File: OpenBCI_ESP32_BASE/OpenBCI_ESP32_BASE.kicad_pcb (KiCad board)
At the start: 2 copper layers, 50 x 50 mm, 43 parts, among them J1 Conn_01x02, J2 Conn_02x03_Odd_Even, J3 Conn_02x02_Odd_Even, J4 Conn_02x08_Odd_Even, SW1 SW_SPST, U1 LIS3DH, U10 TPS72325, U2 ESP32-DevKitC, U8 TPS60403, U9 TPS73225

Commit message: Latest PCB file and firmware
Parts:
- added R1: NF, Resistor_SMD:R_0603_1608Metric, F.Cu at (112.6, 57.8)
- added R2: NF, Resistor_SMD:R_0603_1608Metric, F.Cu at (125.0, 94.0)
- C1, C2, C3: value C -> 10u
- C35, C36, C37, C38, C39, C41, C42, C43: footprint Capacitor_SMD:C_0805_2012Metric -> Capacitor_SMD:C_0603_1608Metric
- C4: value C -> 0.1u; footprint Capacitor_SMD:C_0805_2012Metric -> Capacitor_SMD:C_0603_1608Metric
- J1: footprint Connector_JST:JST_PH_S2B-PH-K_1x02_P2.00mm_Horizontal -> Connector_JST:JST_PH_S2B-PH-SM4-TB_1x02-1MP_P2.00mm_Horizontal
- SW1: value SW_SPST -> SW_SPDT; footprint OpenBCI_ESP32:SW_SPDT_CK-JS102011SAQN -> Button_Switch_SMD:SW_SPDT_CK-JS102011SAQN
- moved J1 2.28 mm to (137.6, 55.1)
- moved C50 1.94 mm to (103.9, 60.8)
- moved C33 1.70 mm to (124.1, 61.1)
- moved C34 1.70 mm to (127.3, 62.3)
- moved L1 1.70 mm to (127.3, 60.3)
- moved D1 1.70 mm to (130.8, 59.6)
- moved SW1 1.70 mm to (126.0, 52.3)
- moved U2 0.40 mm to (148.5, 65.3)
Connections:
- J2 pad 5: Net-(J2-Pad5) -> unconnected-(J2-Pad5)
- J4 pad 12: Net-(J4-Pad12) -> unconnected-(J4-Pad12)
- J4 pad 13: Net-(J4-Pad13) -> unconnected-(J4-Pad13)
- J4 pad 5: Net-(J4-Pad5) -> unconnected-(J4-Pad5)
- J4 pad 7: Net-(J4-Pad7) -> unconnected-(J4-Pad7)
- SW1 pad 3: (no net) -> unconnected-(SW1-Pad3)
- U1 pad 11: Net-(U1-Pad11) -> /OpenBCI_ESP_DEVKIT/INT1
- U1 pad 2: Net-(U1-Pad2) -> unconnected-(U1-Pad2)
- U1 pad 3: Net-(U1-Pad3) -> unconnected-(U1-Pad3)
- U1 pad 7: Net-(U1-Pad7) -> unconnected-(U1-Pad7)
- U1 pad 9: Net-(U1-Pad9) -> unconnected-(U1-Pad9)
- U2 pad 11: Net-(U2-Pad11) -> /OpenBCI_ESP_DEVKIT/INT1
- U2 pad 16: Net-(U2-Pad16) -> unconnected-(U2-Pad16)
- U2 pad 17: Net-(U2-Pad17) -> unconnected-(U2-Pad17)
- U2 pad 18: Net-(U2-Pad18) -> unconnected-(U2-Pad18)
- U2 pad 2: Net-(U2-Pad2) -> unconnected-(U2-Pad2)
- U2 pad 20: Net-(U2-Pad20) -> unconnected-(U2-Pad20)
- U2 pad 21: Net-(U2-Pad21) -> unconnected-(U2-Pad21)
- U2 pad 22: Net-(U2-Pad22) -> unconnected-(U2-Pad22)
- U2 pad 24: Net-(U2-Pad24) -> unconnected-(U2-Pad24)
- U2 pad 25: Net-(U2-Pad25) -> unconnected-(U2-Pad25)
- U2 pad 26: Net-(U2-Pad26) -> unconnected-(U2-Pad26)
- U2 pad 34: Net-(U2-Pad34) -> unconnected-(U2-Pad34)
- U2 pad 35: Net-(U2-Pad35) -> unconnected-(U2-Pad35)
- U2 pad 38: Net-(U2-Pad38) -> GND
- U2 pad 4: Net-(U2-Pad4) -> unconnected-(U2-Pad4)
- U2 pad 5: Net-(U2-Pad5) -> unconnected-(U2-Pad5)
- U2 pad 6: Net-(U2-Pad6) -> unconnected-(U2-Pad6)
- U2 pad 7: Net-(U2-Pad7) -> /OpenBCI_ESP_DEVKIT/SDCD
- U2 pad 8: Net-(U2-Pad8) -> unconnected-(U2-Pad8)
- XS1 pad 1: Net-(XS1-Pad1) -> unconnected-(XS1-Pad1)
- XS1 pad 8: Net-(XS1-Pad8) -> unconnected-(XS1-Pad8)
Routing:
- net /OpenBCI_ESP_DEVKIT/INT1: track 0.00 -> 28.7 mm, vias 0 -> 3
- net /OpenBCI_ESP_DEVKIT/SDCD: track 0.00 -> 24.8 mm, vias 0 -> 1
- net GND: track 127.8 -> 118.4 mm
- net Net-(C42-Pad1): track 7.21 -> 12.4 mm
- net -2V5: track 49.4 -> 45.6 mm
- net Net-(J1-Pad1): track 9.86 -> 12.9 mm
- net Net-(C43-Pad1): track 7.76 -> 10.6 mm
- net Net-(C39-Pad1): track 2.21 -> 4.21 mm
- net +5V: track 39.3 -> 37.4 mm
- net +2V5: track 18.4 -> 16.7 mm
- net Net-(C40-Pad1): track 1.93 -> 3.53 mm
- net +3V3: track 77.6 -> 76.1 mm
- net Net-(C34-Pad1): track 40.8 -> 39.4 mm
- net /OpenBCI_ESP_DEVKIT/SCL: track 18.4 -> 17.6 mm
- net -5V: track 23.9 -> 23.3 mm
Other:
- net class Default removed

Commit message: Firmware updates
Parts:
- added R3: 4k7, Resistor_SMD:R_0603_1608Metric, F.Cu at (133.4, 80.7)
- added R4: 4k7, Resistor_SMD:R_0603_1608Metric, F.Cu at (135.2, 80.7)
- added R5: 220k, Resistor_SMD:R_0603_1608Metric, F.Cu at (137.1, 61.4)
- added R6: 120k, Resistor_SMD:R_0603_1608Metric, F.Cu at (141.1, 61.4)
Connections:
- U2 pad 3: /OpenBCI_ESP_DEVKIT/BATT -> Net-(U2-Pad3)
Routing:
- net Net-(U2-Pad3): track 0.00 -> 7.61 mm
- net +5V: track 37.4 -> 42.9 mm
- net /OpenBCI_ESP_DEVKIT/SDA: track 11.6 -> 15.9 mm
- net +3V3: track 76.1 -> 73.2 mm, vias 4 -> 5
- net /OpenBCI_ESP_DEVKIT/SCL: track 17.6 -> 20.0 mm

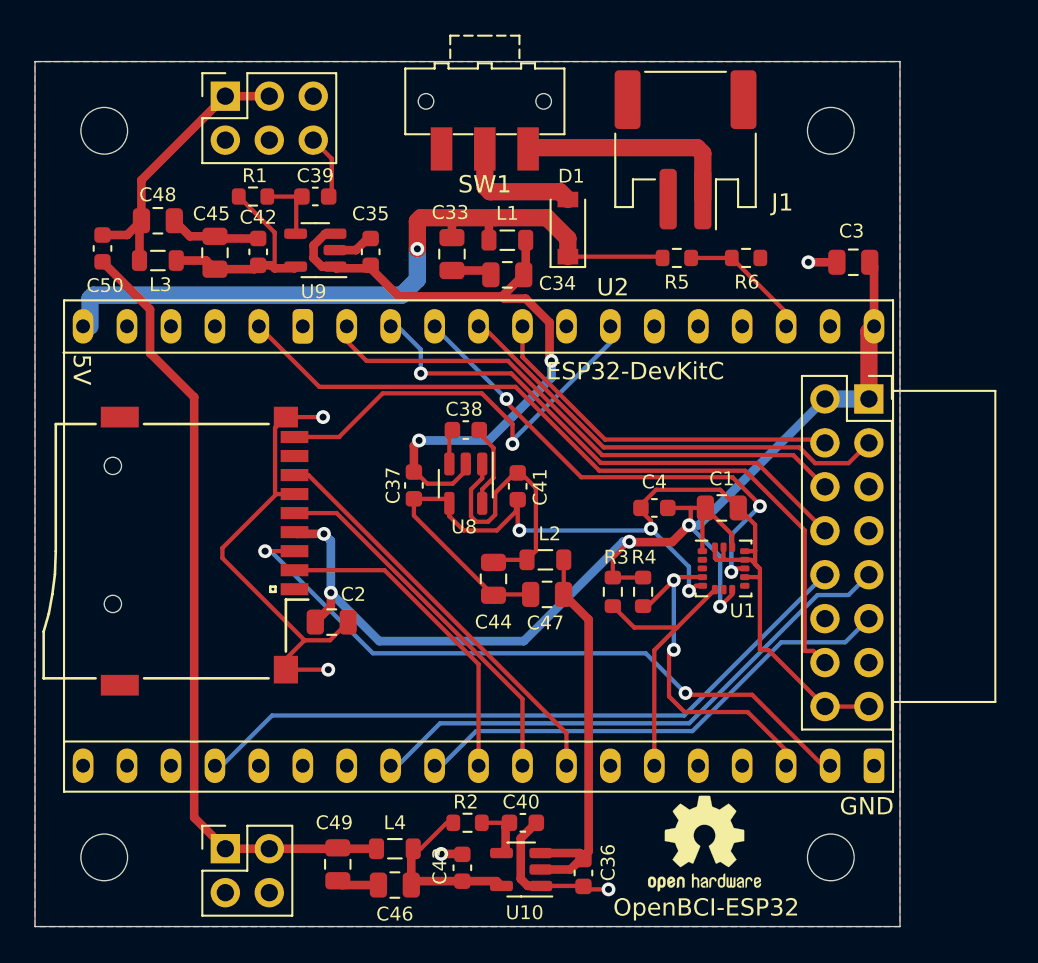
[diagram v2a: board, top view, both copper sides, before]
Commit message: Kicad and firmware updates
Kicad schematic and PCB updates for SD Card issue
Firmware tests for SD card
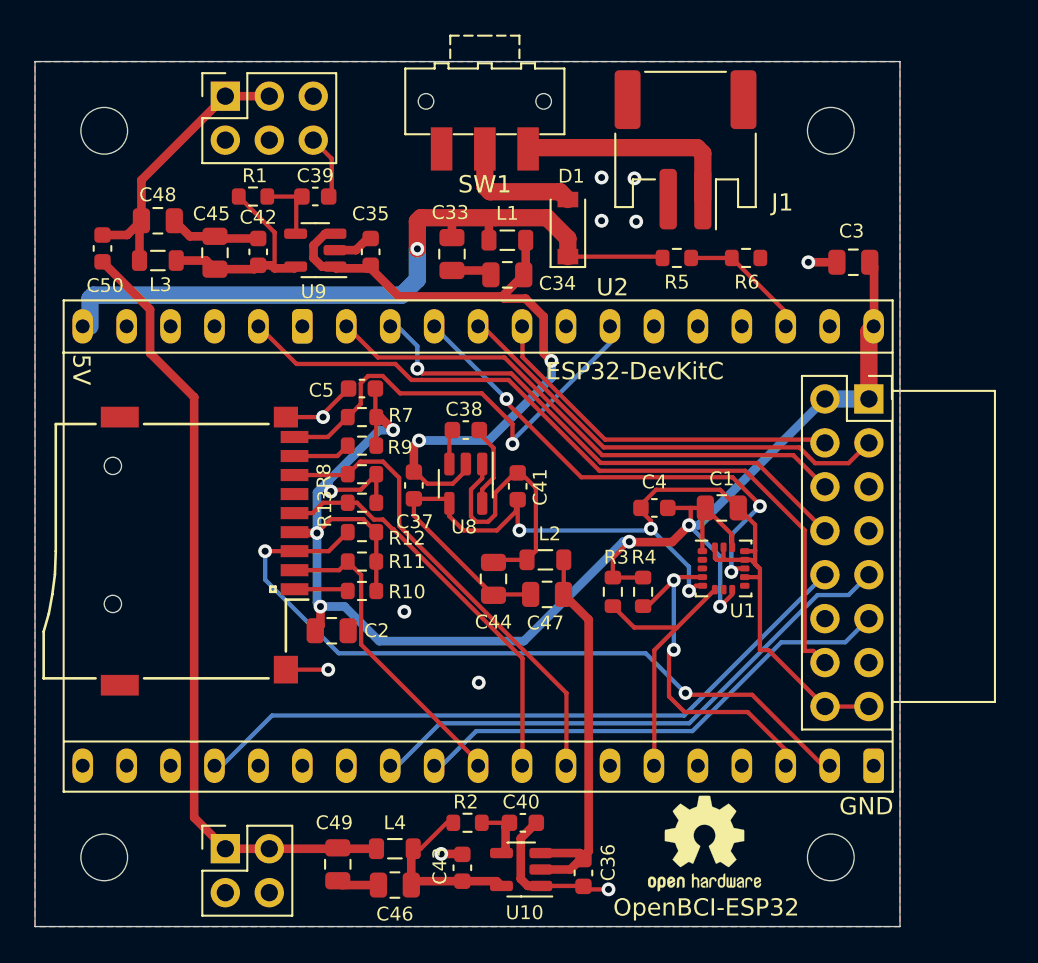
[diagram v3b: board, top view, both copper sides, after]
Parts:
- added C5: 0.1u, Capacitor_SMD:C_0603_1608Metric, F.Cu at (118.9, 68.9)
- added R10: 10k, Resistor_SMD:R_0603_1608Metric, F.Cu at (118.9, 80.6)
- added R11: 10k, Resistor_SMD:R_0603_1608Metric, F.Cu at (118.9, 78.9)
- added R12: 10k, Resistor_SMD:R_0603_1608Metric, F.Cu at (118.9, 77.2)
- added R13: 10k, Resistor_SMD:R_0603_1608Metric, F.Cu at (118.9, 75.5)
- added R7: 10k, Resistor_SMD:R_0603_1608Metric, F.Cu at (118.9, 70.5)
- added R8: 10k, Resistor_SMD:R_0603_1608Metric, F.Cu at (118.9, 73.8)
- added R9: 10k, Resistor_SMD:R_0603_1608Metric, F.Cu at (118.9, 72.2)
- moved C2 0.50 mm to (117.2, 82.9)
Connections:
- XS1 pad 1: unconnected-(XS1-Pad1) -> Net-(XS1-Pad1)
- XS1 pad 8: unconnected-(XS1-Pad8) -> Net-(XS1-Pad8)
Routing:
- net +3V3: track 73.2 -> 98.8 mm, vias 5 -> 7
- net GND: track 118.4 -> 98.1 mm, vias 8 -> 14
- net /OpenBCI_ESP_DEVKIT/SDMOSI: track 39.6 -> 44.0 mm
- net /OpenBCI_ESP_DEVKIT/SDMISO: track 23.8 -> 27.4 mm
- net Net-(XS1-Pad8): track 0.00 -> 3.32 mm
- net Net-(XS1-Pad1): track 0.00 -> 3.12 mm
- net /OpenBCI_ESP_DEVKIT/SDCLK: track 21.5 -> 23.4 mm
- net /OpenBCI_ESP_DEVKIT/SDCD: track 24.8 -> 26.4 mm
- net /OpenBCI_ESP_DEVKIT/SDCS: track 18.8 -> 18.2 mm

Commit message: Code and STL updates
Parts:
- moved L4 2.21 mm to (120.7, 97.7)
- moved C46 1.96 mm to (120.7, 95.7)
- turned C49 to 90 degrees
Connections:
- J2 pad 1: +2V5 -> GND
- J2 pad 2: GND -> +2V5
- J2 pad 3: +2V5 -> GND
- J2 pad 4: GND -> +2V5
- J2 pad 5: unconnected-(J2-Pad5) -> GND
- J2 pad 6: GND -> unconnected-(J2-Pad6)
- J3 pad 1: -2V5 -> GND
- J3 pad 2: GND -> -2V5
- J3 pad 3: -2V5 -> GND
- J3 pad 4: GND -> -2V5
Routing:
- net GND: track 98.1 -> 94.2 mm, vias 14 -> 44
- net -2V5: track 45.6 -> 48.4 mm
- net +2V5: track 16.7 -> 15.6 mm
- net /OpenBCI_ESP_DEVKIT/SDA: track 15.9 -> 16.9 mm

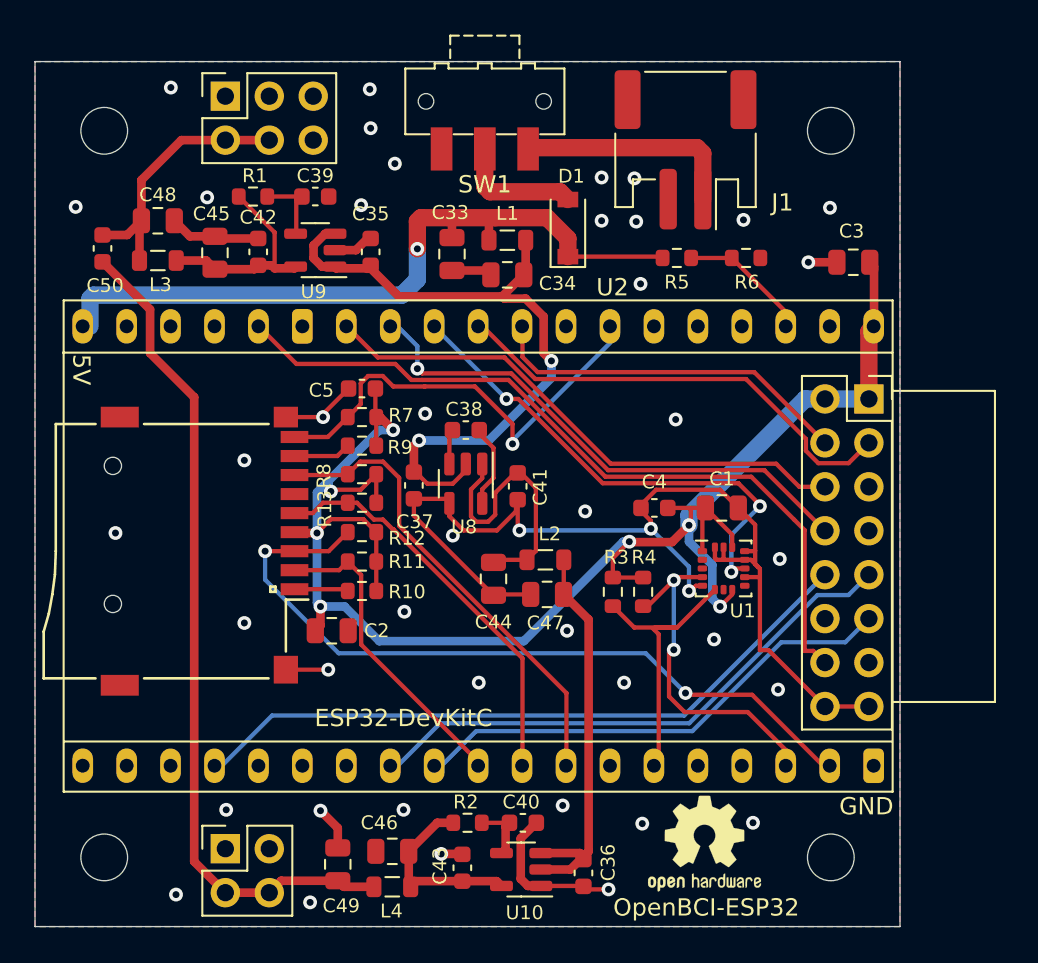
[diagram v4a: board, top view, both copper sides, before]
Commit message: add ADS1298 files
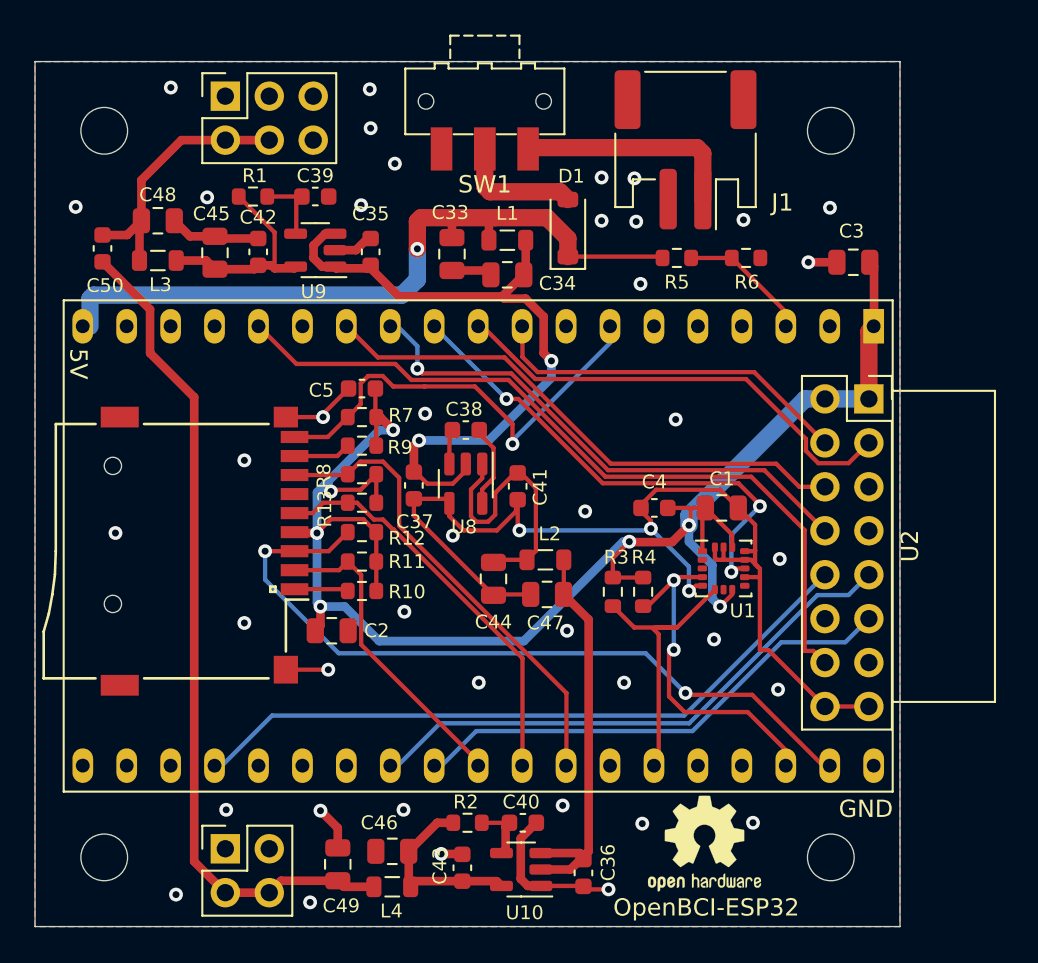
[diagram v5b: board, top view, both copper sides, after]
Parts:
- U2: footprint OpenBCI_ESP32:ESP32-DevKitC -> Espressif:ESP32-DevKitC
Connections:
- net +3V3 renamed +3.3V
- R10 pad 2: Net-(R10-Pad2) -> Net-(XS1-DAT2)
- R9 pad 2: Net-(R9-Pad2) -> Net-(XS1-DAT1)
